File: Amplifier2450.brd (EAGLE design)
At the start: 39.4 x 35.5 mm, 25 parts, among them IC1 7805DT, Q1 P-KANAL_MOSFET_, X1 SMA-142-0701-801/806, X2 SMA-142-0701-801/806

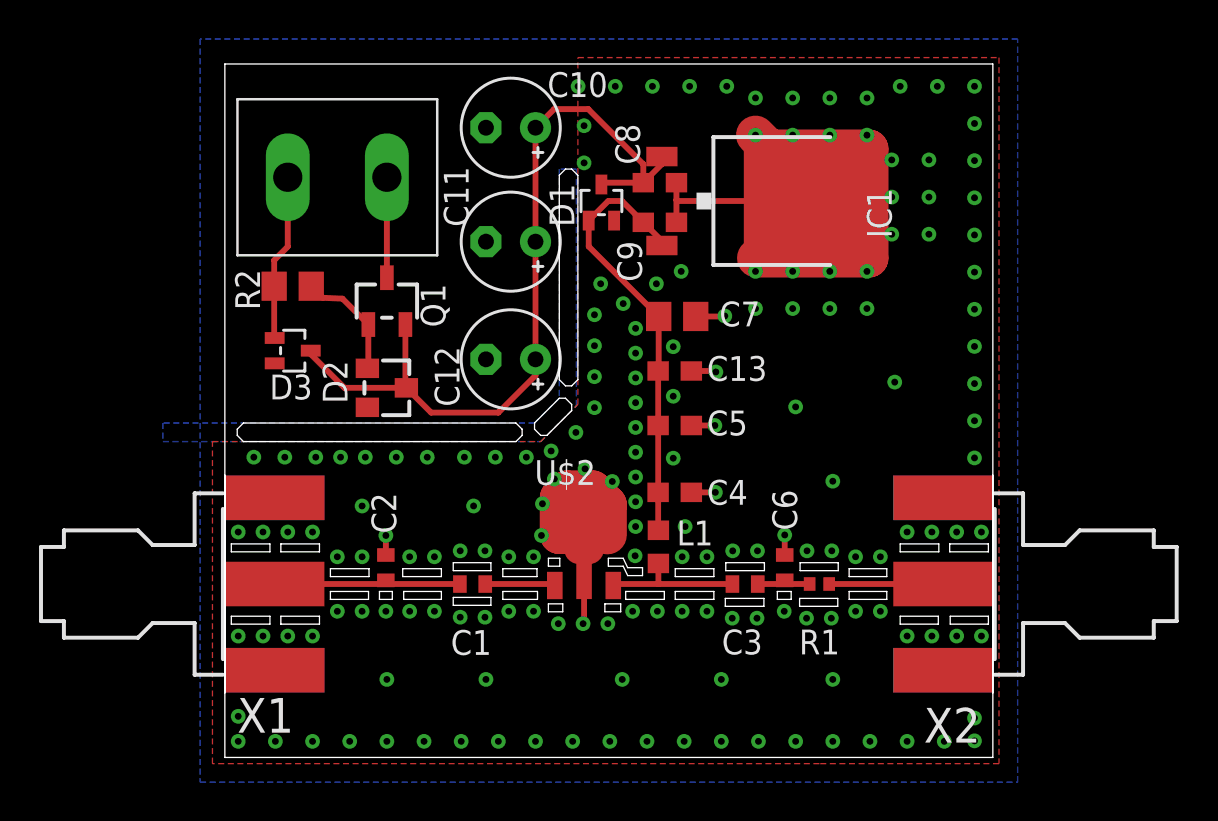
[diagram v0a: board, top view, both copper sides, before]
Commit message: (Tobias): added a top layer ground plane cutout around the signal line to prevent spilling.
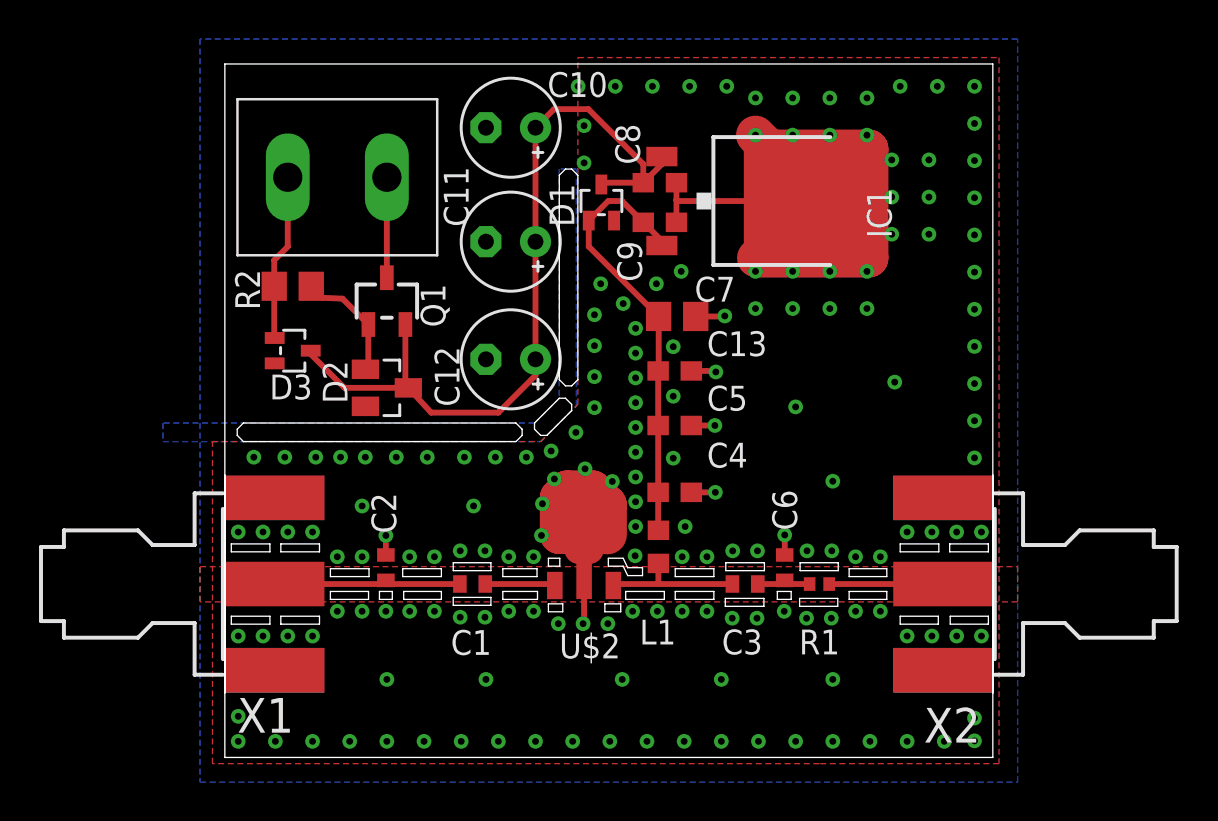
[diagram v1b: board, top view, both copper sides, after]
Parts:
- C10, C11, C12: value 100u -> 10u
- D2: value BZX84CSMD -> 5,1V; device diode:TO236 -> diode:SOT23
- R2: value (none) -> 4k7
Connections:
- net +15V: now also D2.3; no longer D2.C
- net N$7: now also D2.1; no longer D2.A
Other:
- board text added: "Cutout between power connector and amplifier. The Ground and power lines shall be defined primaraly by the analoge DC-DC Converter. The powerlines shall only connect in a single star point"
- board text added: "Starpoint of the power planes/lines to minimize potential loop area."
- board text added: "Use thermals around the signal connectors/pads to minimize thermal coupling with other devices"
- board text removed: "Cutout between power connector and amplifier. The Ground and power lines shall be defined primaraly by the analoge DC-DC Converter. The Powerlines shall only connect in a star point"
- board text removed: "Starpoint of the power planes/lines"
